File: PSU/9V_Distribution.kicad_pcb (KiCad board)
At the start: 2 copper layers, 70 x 80 mm, 29 parts, among them J1 Screw_Terminal_2_P5.00mm, J2 Screw_Terminal_2_P5.00mm, J3 Screw_Terminal_2_P5.00mm, J4 Screw_Terminal_2_P5.00mm, J5 Screw_Terminal_2_P5.00mm, U1 P78A05-1000, U4 LM2596S-5

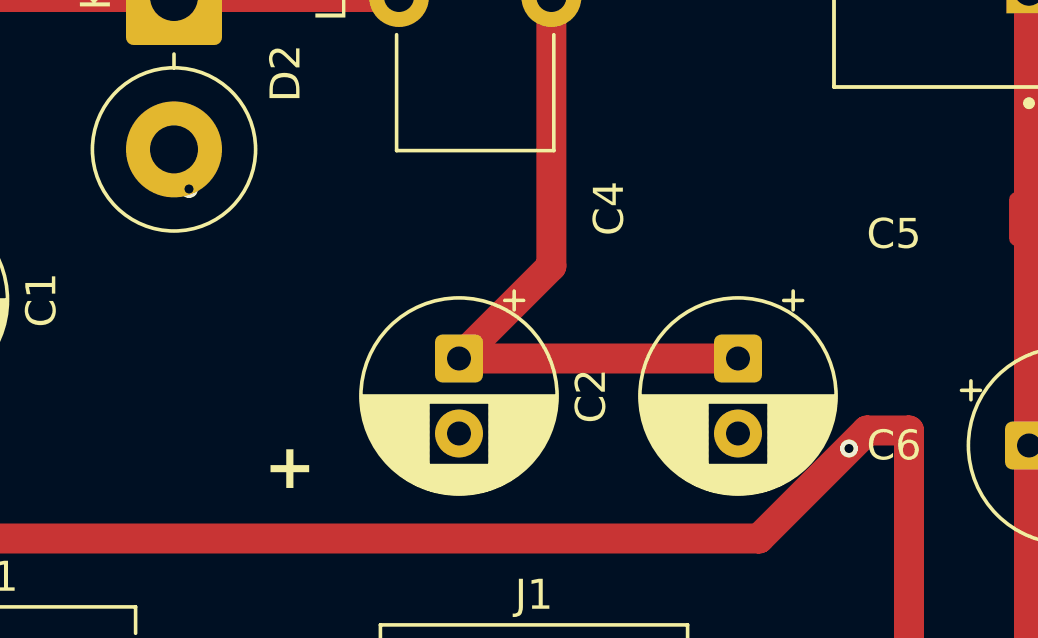
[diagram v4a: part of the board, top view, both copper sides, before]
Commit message: Refill the PSU zones and drop two stray vias
Zones refilled in Pcbnew after the through-hole conversion. That left two
vias dangling:

  (129.0, 71.35)  a stitching via for D2's old anode position. D2's anode is
                  now a through-hole pad 1.3mm away that reaches both planes
                  by itself, so the via has nothing to do.
  (151.0, 80.0)   a ground stitching via that the re-routed 9V branch now
                  runs exactly over, so KiCad had reassigned it to
                  Net-(D1-K). Not a short, but a pointless hole in the
                  ground plane.

Both removed. The board is now at 12 violations, all library links: three
LED footprints from the missing Alternate KiCad Library and nine version
drifts against stock footprints. 0 unconnected items, 0 schematic parity
issues.

Removing the vias leaves two small unfilled circles in the pour where their
clearance used to be. Harmless, and they close on the next refill.

Co-Authored-By: Claude Opus 5 <noreply@anthropic.com>
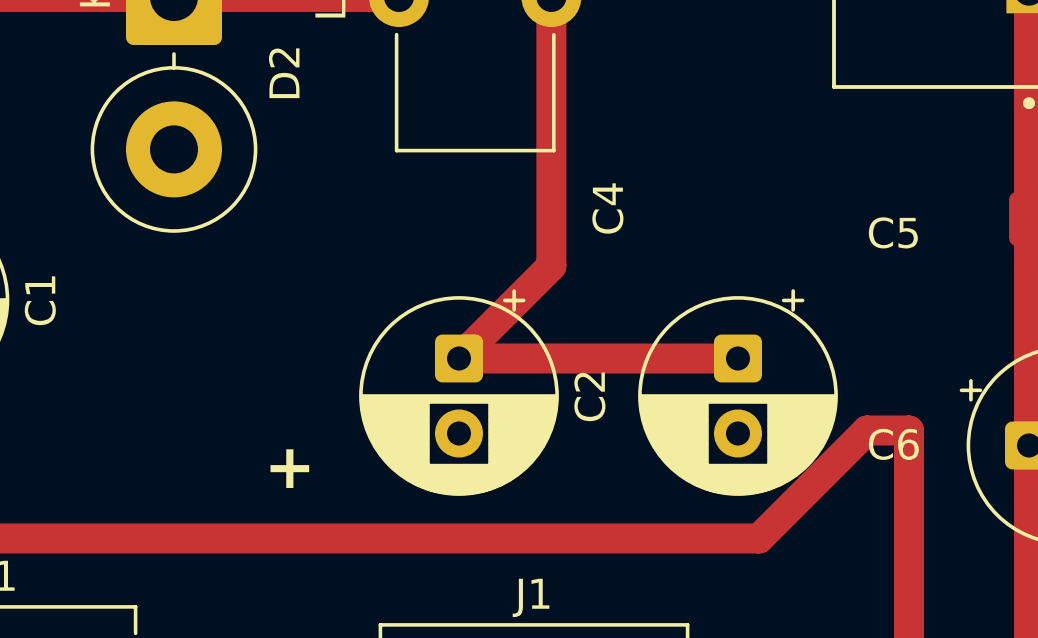
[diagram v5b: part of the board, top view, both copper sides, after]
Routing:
- net GND: vias 17 -> 15
